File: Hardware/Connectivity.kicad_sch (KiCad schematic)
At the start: 77 parts, among them J11 USB4235-03-C_REVA, J13 USB_A, J17 Conn_01x04, J19 Conn_02x13_Counter_Clockwise, J2 Conn_01x02, J3 Conn_01x02, J4 Conn_01x02, J7 FTSH-107-01-L-D-K, J8 Conn_01x02, J9 Conn_01x02, Q3 DMT6018LDR-7, Q4 DMT6018LDR-7, Q5 DMT6018LDR-7, Q6 DMT6018LDR-7, Q7 DMT6018LDR-7, SW1 SW_Push, U4 MCP2542FD-E/MF

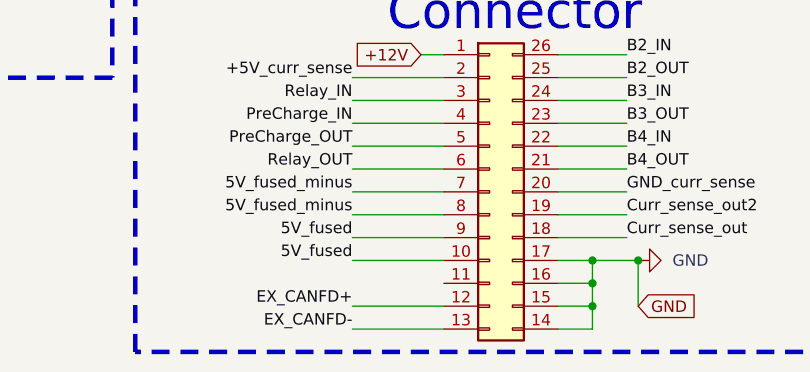
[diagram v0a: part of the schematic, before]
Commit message: Zmieniono złącza, zmieniono kondensatory na kondensatory bezpieczeństwa, poprawiono masę oraz dodano podział na hardware i software
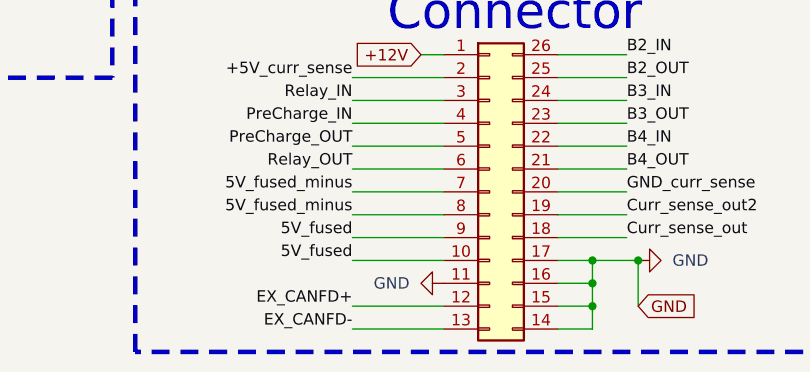
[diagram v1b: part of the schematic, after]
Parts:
- J19: footprint footrpint:HARWIN_M80-5402642 -> footrpint:HARWIN_M80-5002642
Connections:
- net GND: now also J19.11 (Pin_11)
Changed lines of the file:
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@@
+	)
+	(symbol
+		(lib_id "power:GND")
+		(at 143.51 158.75 270)
+		(unit 1)
+		(exclude_from_sim no)
+		(in_bom yes)
+		(on_board yes)
+		(dnp no)
+		(fields_autoplaced yes)
+		(property "Reference" "#PWR033"
+			(at 137.16 158.75 0)
+			(effects
+				(font
+					(size 1.27 1.27)
+				)
+				(hide yes)
+			)
+		)
+		(property "Value" "GND"
+			(at 139.7 158.7499 90)
+			(effects
+				(font
+					(size 1.27 1.27)
+				)
+				(justify right)
+			)
+		)
+		(property "Footprint" ""
+			(at 143.51 158.75 0)
+			(effects
+				(font
+					(size 1.27 1.27)
+				)
+				(hide yes)
+			)
+		)
+		(property "Datasheet" ""
+			(at 143.51 158.75 0)
+			(effects
+				(font
+					(size 1.27 1.27)
+				)
+				(hide yes)
+			)
+		)
+		(property "Description" "Power symbol creates a global label with name \"GND\" , ground"
+			(at 143.51 158.75 0)
+			(effects
+				(font
+					(size 1.27 1.27)
+				)
+				(hide yes)
+			)
+		)
+		(pin "1"
+		)
+		(instances
+			(project "BMS"
+				(path "/26289bb6-56bc-4ca1-b1a2-18d58d1afdf5/d34f5976-9b74-4159-94dc-792c476298a2"
+					(reference "#PWR033")
+					(unit 1)
+				)
+			)
+		)
 	)
 	(symbol
@@
 			)
 		)
-		(property "Footprint" "footrpint:HARWIN_M80-5402642"
+		(property "Footprint" "footrpint:HARWIN_M80-5002642"
 			(at 148.59 148.59 0)
 			(effects
@@
 			)
 		)
-		(property "Datasheet" "https://www.harwin.com/products/M80-5402642"
+		(property "Datasheet" "https://www.harwin.com/products/M80-5002642"
 			(at 148.59 148.59 0)
 			(effects

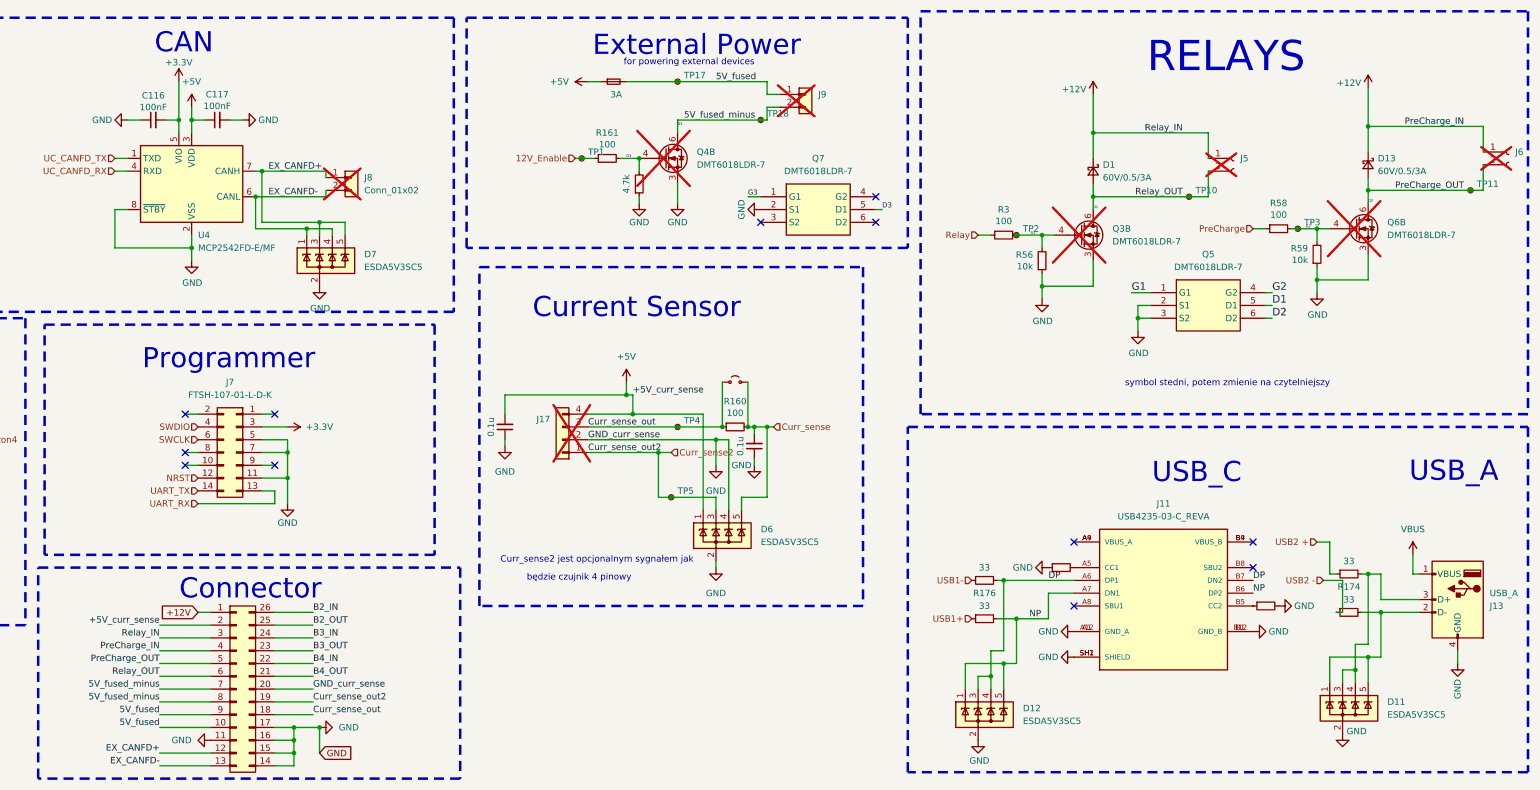
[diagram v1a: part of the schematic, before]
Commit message: Dodano diody TVS na każdej części zasilania, zmieniono bezpieczniki, podzielono bezpieczniki na bezpieczniki do prądów wewnętrznych oraz zewnętrznych,poprawiono małe błedy
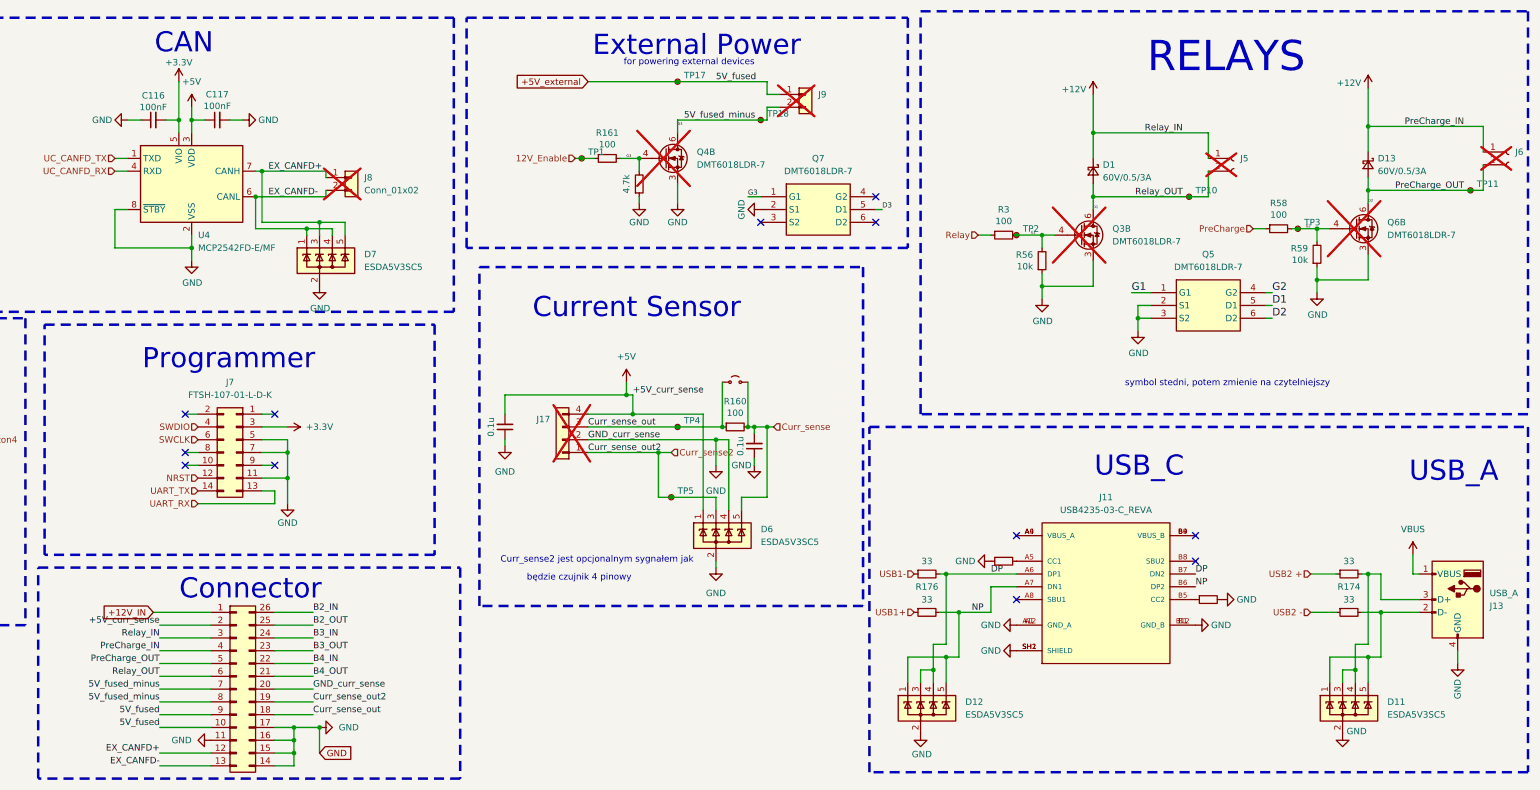
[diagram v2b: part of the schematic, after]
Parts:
- removed F1: 3A, Fuse:Fuse_0603_1608Metric_Pad1.05x0.95mm_HandSolder, symbol Device:Fuse_Small
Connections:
- net +12V: no longer J19.1 (Pin_1)
- net 5V_fused renamed +5V_external
- new net +12V_IN: J19.1 (Pin_1)
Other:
- moved on the sheet: D12, J11, R176

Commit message: Dodano wyjaśnienia w schemacie, zmieniono nazewnictwo wewnętrzne lini can
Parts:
- added J20: Conn_01x04, footrpint:HARWIN_M80-5100442, symbol Connector_Generic:Conn_01x04
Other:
- note added: "DMT6018LDR-7 is a package with 2 mossfets inside."
- note added: "Explanation:"
- note added: "Meaning that its connected to external connector in reality there is no 4 pin connector but the connection is on a bigger 26 pin with other signals."
- note added: "Some of the items are crossed out, the crossed out items are ment to show how the elements are connected, in reality the components are connected to another footrpint that does that function. For example:"
- note added: "The connection is on the main connector"
- note removed: "symbol stedni, potem zmienie na czytelniejszy"
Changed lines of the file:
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@@
 	)
 	(rectangle
+		(start 312.42 171.45)
+		(end 405.13 250.19)
+		(stroke
+			(width 0.5)
+			(type dash)
+			(color 0 0 0 1)
+		)
+		(fill
+			(type none)
+		)
+	)
+	(rectangle
 		(start 100.33 15.24)
 		(end 191.77 73.66)
@@
 		)
 	)
+	(text "Some of the items are crossed out, the crossed \nout items are ment to show how the elements \nare connected, in reality the components\nare connected to another footrpint that \ndoes that function. For example:"
+		(exclude_from_sim no)
+		(at 358.14 196.85 0)
+		(effects
+			(font
+				(size 2 2)
+				(color 0 0 0 1)
+			)
+		)
+	)
 	(text "będzie czujnik 4 pinowy\n"
 		(exclude_from_sim no)
@@
 		)
 	)
+	(text "Meaning that its connected to external connector\nin reality there is no 4 pin connector but the\nconnection is on a bigger 26 pin with other signals."
+		(exclude_from_sim no)
+		(at 359.41 224.79 0)
+		(effects
+			(font
+				(size 2 2)
+				(color 0 0 0 1)
+			)
+		)
+	)
 	(text "USB_A \n"
 		(exclude_from_sim no)
@@
 		)
 	)
-	(text "symbol stedni, potem zmienie na czytelniejszy\n"
+	(text "DMT6018LDR-7 is a package with 2 mossfets inside.\n"
 		(exclude_from_sim no)
 		(at 345.44 87.884 0)
@@
 		)
 	)
+	(text "The connection is on the main connector"
+		(exclude_from_sim no)
+		(at 57.15 128.27 0)
+		(effects
+			(font
+				(size 1.27 1.27)
+			)
+		)
+	)
 	(text "External Power\n"
 		(exclude_from_sim no)
@@
 		)
 	)
+	(text "Explanation:"
+		(exclude_from_sim no)
+		(at 358.14 179.07 0)
+		(effects
+			(font
+				(size 5 5)
+				(thickness 0.625)
+				(color 0 0 0 1)
+			)
+		)
+	)
 	(text "RELAYS"
 		(exclude_from_sim no)
@@
 					(unit 1)
 				)
+			)
+		)
+	)
+	(symbol
+		(lib_id "Connector_Generic:Conn_01x04")
+		(at 356.87 213.36 180)
+		(unit 1)
+		(exclude_from_sim no)
+		(in_bom no)
+		(on_board no)
+		(dnp yes)
+		(property "Reference" "J20"
+			(at 353.06 209.296 0)
+			(effects
+				(font
+					(size 1.27 1.27)
+				)
+			)
+		)
+		(property "Value" "Conn_01x04"
+			(at 356.616 205.74 0)
+			(effects
+				(font
+					(size 1.27 1.27)
+				)
+				(hide yes)
+			)
+		)
+		(property "Footprint" "footrpint:HARWIN_M80-5100442"
+			(at 356.87 213.36 0)
+			(effects
+				(font
+					(size 1.27 1.27)
+				)
+				(hide yes)
+			)
+		)
+		(property "Datasheet" "~"
+			(at 356.87 213.36 0)
+			(effects
+				(font
+					(size 1.27 1.27)
+				)
+				(hide yes)
+			)
+		)
+		(property "Description" "Generic connector, single row, 01x04, script generated (kicad-library-utils/schlib/autogen/connector/)"
+			(at 356.87 213.36 0)
+			(effects
+				(font
+					(size 1.27 1.27)
+				)
+				(hide yes)
+			)
+		)
+		(pin "4"
+		)
+		(pin "1"
+		)
+		(pin "2"
+		)
+		(pin "3"
+		)
+		(instances
+			(project "BMS"
+				(path "/26289bb6-56bc-4ca1-b1a2-18d58d1afdf5/d34f5976-9b74-4159-94dc-792c476298a2"
+					(reference "J20")
+					(unit 1)
+				)

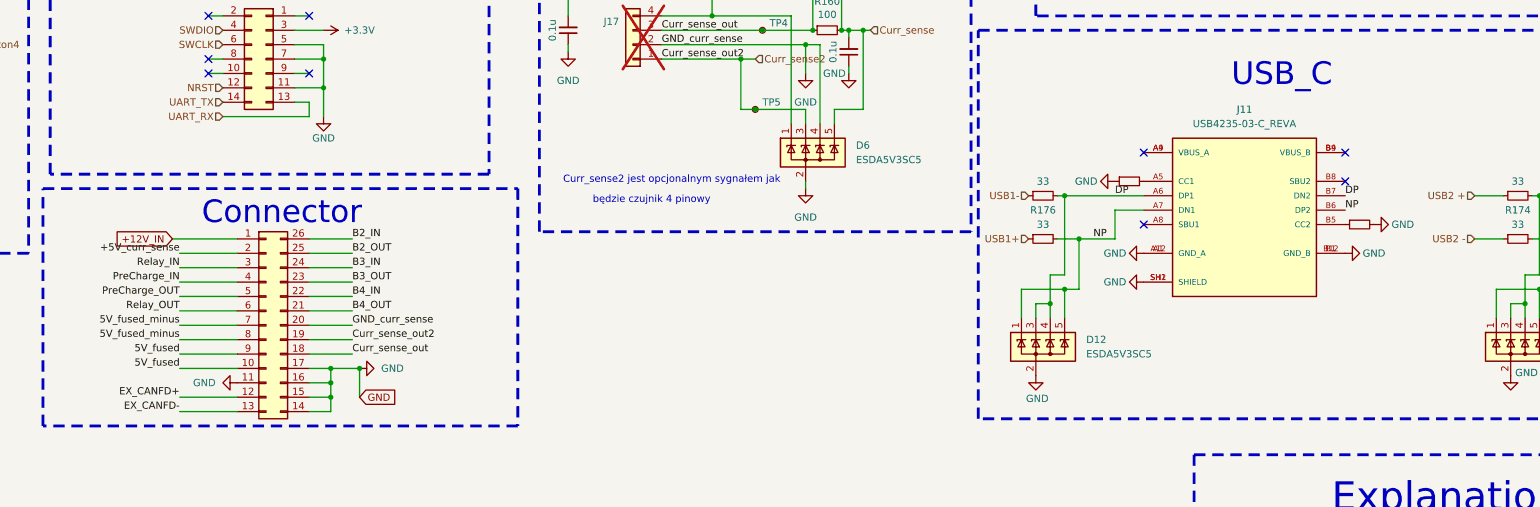
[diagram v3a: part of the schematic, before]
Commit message: dodano pozostale datasheety, zmieniono blad w usb
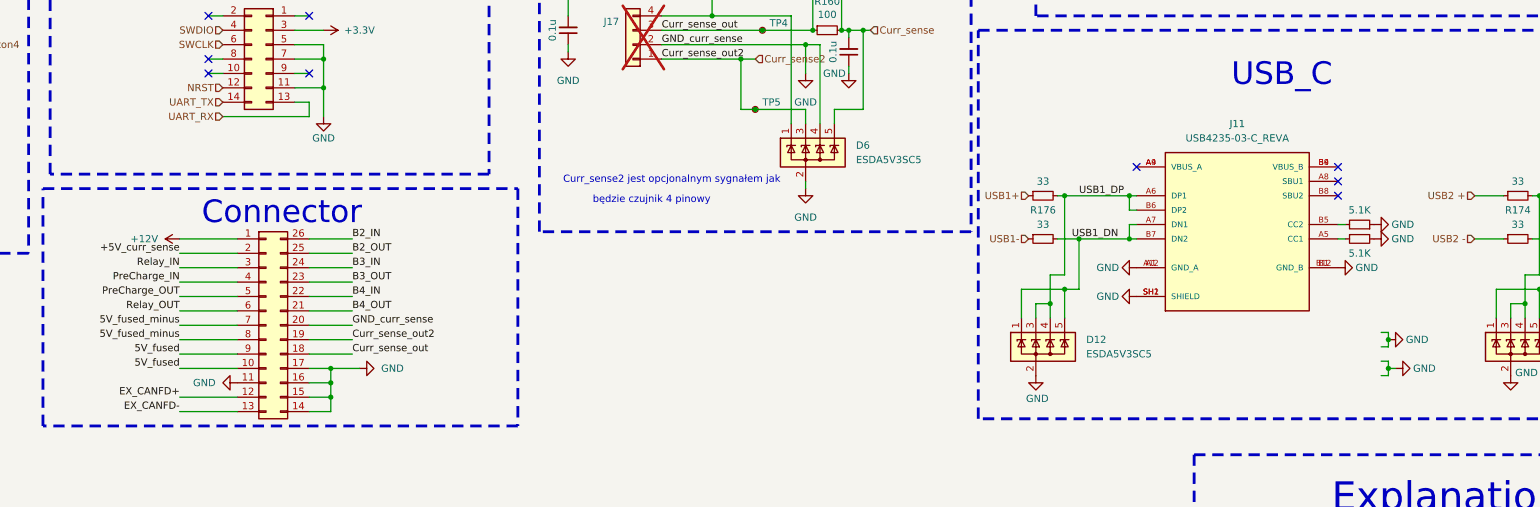
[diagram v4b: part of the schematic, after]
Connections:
- net +12V_IN is gone; now on net +12V: J19.1 (Pin_1)
- net USB1+: now also R175.1; no longer R176.1
- net USB1-: now also R176.1; no longer R175.1
- net at R76.1: now also J11.A5 (CC1); no longer J11.B5 (CC2)
- net at R75.2: now also J11.B5 (CC2); no longer J11.A5 (CC1)
- net DP renamed USB1_DP
- net USB1_DP: now also J11.B6 (DP2); no longer J11.B7 (DN2)
- net NP renamed USB1_DN
- net USB1_DN: now also J11.B7 (DN2); no longer J11.B6 (DP2)
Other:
- moved on the sheet: J11

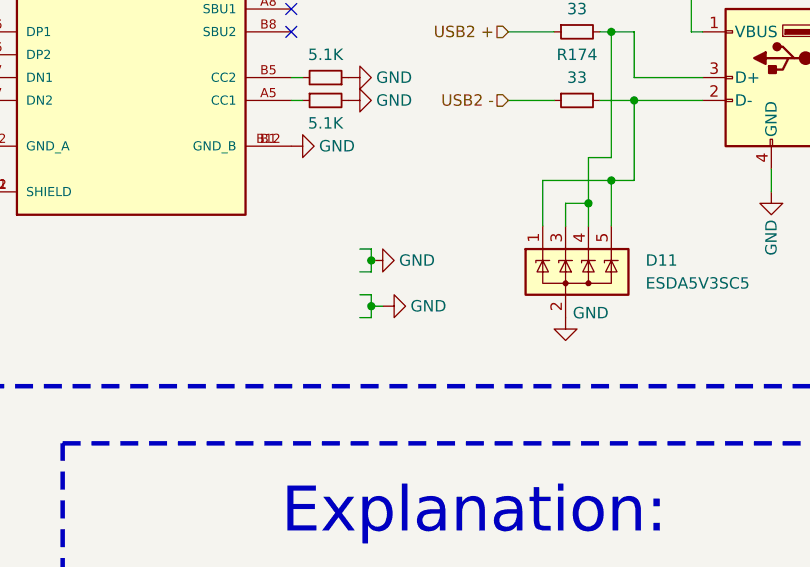
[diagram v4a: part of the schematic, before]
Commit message: Zmiany wizualne na płytce, poprawiono ulozenie elementow na masce dekoracyjnej
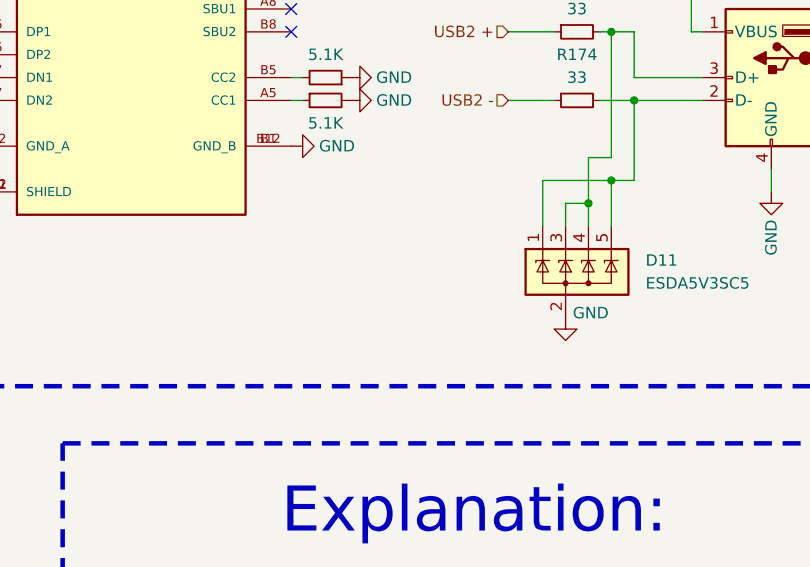
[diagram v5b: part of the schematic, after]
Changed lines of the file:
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@@
 	)
 	(junction
-		(at 346.71 151.13)
-		(diameter 0)
-		(color 0 0 0 0)
-	)
-	(junction
 		(at 217.17 43.18)
 		(diameter 0)
@@
 	)
 	(junction
-		(at 346.71 156.21)
-		(diameter 0)
-		(color 0 0 0 0)
-	)
-	(junction
 		(at 66.04 97.79)
 		(diameter 0)
@@
 	(wire
 		(pts
-			(xy 346.71 149.86) (xy 346.71 151.13)
-		)
-		(stroke
-			(width 0)
-			(type default)
-		)
-	)
-	(wire
-		(pts
 			(xy 396.24 44.45) (xy 396.24 49.53)
 		)
@@
 	(wire
 		(pts
-			(xy 345.44 152.4) (xy 346.71 152.4)
-		)
-		(stroke
-			(width 0)
-			(type default)
-		)
-	)
-	(wire
-		(pts
 			(xy 31.75 95.25) (xy 31.75 97.79)
 		)
@@
 	(wire
 		(pts
-			(xy 346.71 157.48) (xy 345.44 157.48)
-		)
-		(stroke
-			(width 0)
-			(type default)
-		)
-	)
-	(wire
-		(pts
 			(xy 215.9 43.18) (xy 217.17 43.18)
 		)
@@
 	(wire
 		(pts
-			(xy 346.71 156.21) (xy 346.71 157.48)
-		)
-		(stroke
-			(width 0)
-			(type default)
-		)
-	)
-	(wire
-		(pts
-			(xy 347.98 156.21) (xy 346.71 156.21)
-		)
-		(stroke
-			(width 0)
-			(type default)
-		)
-	)
-	(wire
-		(pts
 			(xy 326.39 69.85) (xy 330.2 69.85)
 		)
@@
 	(wire
 		(pts
-			(xy 346.71 152.4) (xy 346.71 151.13)
-		)
-		(stroke
-			(width 0)
-			(type default)
-		)
-	)
-	(wire
-		(pts
 			(xy 288.29 125.73) (xy 289.56 125.73)
 		)
@@
 	(wire
 		(pts
-			(xy 345.44 149.86) (xy 346.71 149.86)
-		)
-		(stroke
-			(width 0)
-			(type default)
-		)
-	)
-	(wire
-		(pts
 			(xy 218.44 27.94) (xy 236.22 27.94)
 		)
@@
 	(wire
 		(pts
-			(xy 345.44 154.94) (xy 346.71 154.94)
-		)
-		(stroke
-			(width 0)
-			(type default)
-		)
-	)
-	(wire
-		(pts
 			(xy 156.21 153.67) (xy 163.83 153.67)
 		)
@@
 	(wire
 		(pts
-			(xy 346.71 154.94) (xy 346.71 156.21)
-		)
-		(stroke
-			(width 0)
-			(type default)
-		)
-	)
-	(wire
-		(pts
 			(xy 373.38 139.7) (xy 373.38 125.73)
 		)
@@
 	)
 	(symbol
-		(lib_name "GND_28")
-		(lib_id "power:GND")
-		(at 347.98 156.21 90)
-		(mirror x)
-		(unit 1)
-		(exclude_from_sim no)
-		(in_bom yes)
-		(on_board yes)
-		(dnp no)
-		(property "Reference" "#PWR0142"
-			(at 354.33 156.21 0)
-			(effects
-				(font
-					(size 1.27 1.27)
-				)
-				(hide yes)
-			)
-		)
-		(property "Value" "GND"
-			(at 353.06 156.21 90)
-			(effects
-				(font
-					(size 1.27 1.27)
-				)
-			)
-		)
-		(property "Footprint" ""
-			(at 347.98 156.21 0)
-			(effects
-				(font
-					(size 1.27 1.27)
-				)
-				(hide yes)
-			)
-		)
-		(property "Datasheet" ""
-			(at 347.98 156.21 0)
-			(effects
-				(font
-					(size 1.27 1.27)
-				)
-				(hide yes)
-			)
-		)
-		(property "Description" ""
-			(at 347.98 156.21 0)
-			(effects
-				(font
-					(size 1.27 1.27)
-				)
-				(hide yes)
-			)
-		)
-		(pin "1"
-		)
-		(instances
-			(project "BMS"
-				(path "/26289bb6-56bc-4ca1-b1a2-18d58d1afdf5/d34f5976-9b74-4159-94dc-792c476298a2"
-					(reference "#PWR0142")
-					(unit 1)
-				)
-			)
-		)
-	)
-	(symbol
 		(lib_id "Device:C_Small")
 		(at 31.75 104.14 180)
@@
 					(unit 1)
 				)
-			)
-		)
-	)
-	(symbol
-		(lib_name "GND_28")
-		(lib_id "power:GND")
-		(at 346.71 151.13 90)
-		(mirror x)
-		(unit 1)
-		(exclude_from_sim no)
-		(in_bom yes)
-		(on_board yes)
-		(dnp no)
-		(property "Reference" "#PWR0144"
-			(at 353.06 151.13 0)
-			(effects
-				(font
-					(size 1.27 1.27)
-				)
-				(hide yes)
-			)
-		)
-		(property "Value" "GND"
-			(at 351.79 151.13 90)
-			(effects
-				(font
-					(size 1.27 1.27)
-				)
-			)
-		)
-		(property "Footprint" ""
-			(at 346.71 151.13 0)
-			(effects
-				(font
-					(size 1.27 1.27)
-				)
-				(hide yes)
-			)
-		)
-		(property "Datasheet" ""
-			(at 346.71 151.13 0)
-			(effects
-				(font
-					(size 1.27 1.27)
-				)
-				(hide yes)
-			)
-		)
-		(property "Description" ""
-			(at 346.71 151.13 0)
-			(effects
-				(font
-					(size 1.27 1.27)
-				)
-				(hide yes)
-			)
-		)
-		(pin "1"
-		)
-		(instances
-			(project "BMS"
-				(path "/26289bb6-56bc-4ca1-b1a2-18d58d1afdf5/d34f5976-9b74-4159-94dc-792c476298a2"
-					(reference "#PWR0144")
-					(unit 1)
-				)

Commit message: Wiecej zmian wizualnych pod produkcje
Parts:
- added D10, D14, D18: LED, LED_SMD:LED_0603_1608Metric, symbol Device:LED_Small_ALT
- added R155, R164: 300, Resistor_SMD:R_0603_1608Metric_Pad0.98x0.95mm_HandSolder, symbol Device:R_Small
- added R162: 130, Resistor_SMD:R_0603_1608Metric_Pad0.98x0.95mm_HandSolder, symbol Device:R_Small
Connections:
- net +12V: now also D18.2 (A); no longer J19.1 (Pin_1)
- net +3.3V: now also D14.2 (A)
- net +5V: now also D10.2 (A)
- net GND: now also R155.1, R162.1, R164.1
- new net: D10.1 (K), R155.2
- new net: D18.1 (K), R164.2
- new net: D14.1 (K), R162.2
- new net 12V_IN: J19.1 (Pin_1)
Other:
- note added: "12V status diode"
- note added: "3.3V status diode"
- note added: "5V status diode"
